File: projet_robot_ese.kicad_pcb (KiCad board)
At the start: 4 copper layers, 140 x 40 mm, 114 parts, among them J201 Conn_01x02, J202 Conn_01x04, J203 Conn_01x04, J204 Conn_01x04, J301 Conn_01x06, J302 Conn_01x06, J401 Conn_02x07_Odd_Even, J402 Conn_01x02, J403 Conn_01x02, J404 Conn_01x07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

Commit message: Last commit
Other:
- board text added: "RX"
- board text added: "TX"
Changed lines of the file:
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@@
     (property "Sheetname" "Stm32")
     (attr smd)
-    (fp_text reference "D404" (at 0 -1.43) (layer "F.SilkS")
+    (fp_text reference "D404" (at 0 -1.43) (layer "F.SilkS") hide
       (effects (font (size 1 1) (thickness 0.15)))
     )
@@
     (property "Sheetname" "Stm32")
     (attr smd)
-    (fp_text reference "D405" (at -0.046589 1.379618) (layer "F.SilkS")
+    (fp_text reference "D405" (at -0.046589 1.379618) (layer "F.SilkS") hide
       (effects (font (size 1 1) (thickness 0.15)))
     )
@@
     (property "Sheetname" "Stm32")
     (attr smd)
-    (fp_text reference "R413" (at 0 -1.43) (layer "F.SilkS")
+    (fp_text reference "R413" (at 0 -1.43) (layer "F.SilkS") hide
       (effects (font (size 1 1) (thickness 0.15)))
     )
@@
     (property "Sheetname" "Stm32")
     (attr smd)
-    (fp_text reference "R414" (at 0 1.5) (layer "F.SilkS")
+    (fp_text reference "R414" (at 0 1.5) (layer "F.SilkS") hide
       (effects (font (size 1 1) (thickness 0.15)))
     )
@@
   (gr_line (start 177 94.75) (end 177 103) (layer "F.SilkS") (width 0.15))
   (gr_rect (start 143 90) (end 148 92) (layer "F.SilkS") (width 0.15) (fill solid))
+  (gr_rect (start 141 109.75) (end 145 108.25) (layer "F.SilkS") (width 0.15) (fill solid))
   (gr_rect (start 192.5 116.75) (end 196.5 115.25) (layer "F.SilkS") (width 0.15) (fill solid))
   (gr_rect (start 129.75 111) (end 132.75 113) (layer "F.SilkS") (width 0.15) (fill solid))
@@
   (gr_rect (start 206.5 96) (end 208 100) (layer "F.SilkS") (width 0.15) (fill solid))
   (gr_rect (start 192.5 106.25) (end 196.5 104.75) (layer "F.SilkS") (width 0.15) (fill solid))
+  (gr_rect (start 146 109.75) (end 150 108.25) (layer "F.SilkS") (width 0.15) (fill solid))
   (gr_rect (start 201.5 106.25) (end 205.5 104.75) (layer "F.SilkS") (width 0.15) (fill solid))
   (gr_rect (start 192.5 111.5) (end 196.5 110) (layer "F.SilkS") (width 0.15) (fill solid))
@@
     (effects (font (size 1 1) (thickness 0.15)))
   )
+  (gr_text "TX" (at 148 109) (layer "F.Mask")
+    (effects (font (size 1 1) (thickness 0.15)))
+  )
   (gr_text "LED3" (at 207.25 98 90) (layer "F.Mask")
     (effects (font (size 1 1) (thickness 0.15)))
@@
     (effects (font (size 1 1) (thickness 0.15)))
   )
+  (gr_text "RX" (at 143 109) (layer "F.Mask")
+    (effects (font (size 1 1) (thickness 0.15)))
+  )

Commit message: Prof approved commit
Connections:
- net Net-(J201-Pad2) renamed /Power/BAT_IN
- net VBAT renamed UP_VBAT
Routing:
- net OUT1_1: track 8.55 -> 10.3 mm
- net /Driver moteur/V_BAT: track 150.7 -> 152.4 mm
- net STLINK_RX: track 46.2 -> 44.8 mm
- net GND: track 63.3 -> 62.6 mm
- net Net-(J302-Pad4): track 23.6 -> 23.0 mm
- net Net-(J301-Pad3): track 23.3 -> 24.0 mm
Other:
- board text added: "1"
- board text added: "2"
- board text added: "LED RX"
- board text added: "LED TX"
- board text removed: "COLOR"
- board text removed: "RX"
- board text removed: "TX"

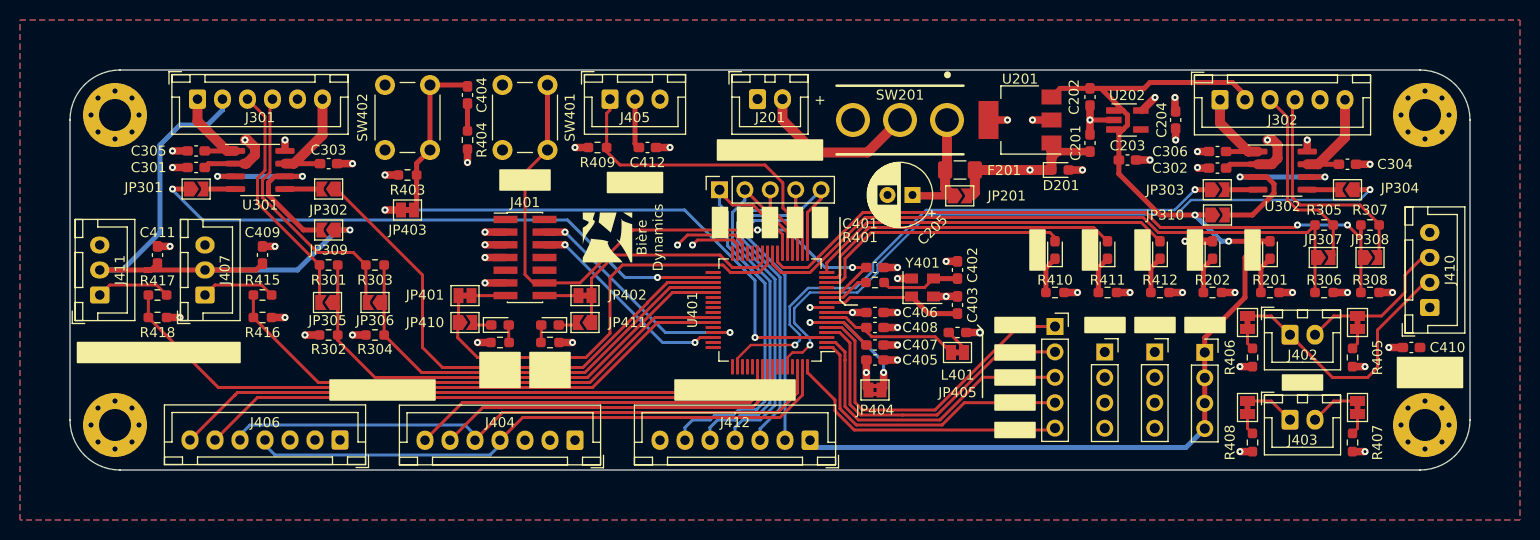
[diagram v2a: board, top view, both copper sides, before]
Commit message: I2C bus correction & simplifaction
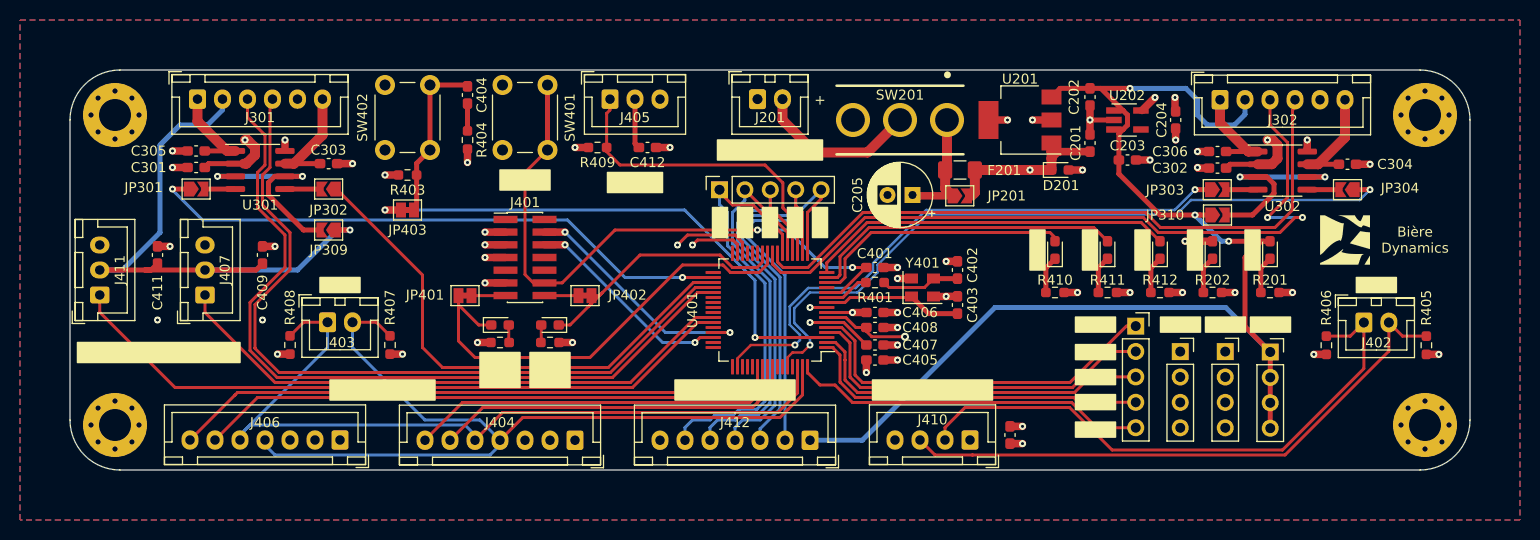
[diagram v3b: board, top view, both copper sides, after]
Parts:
- removed JP305, JP306, JP307, JP308, JP410, JP411: SolderJumper_2_Open, Jumper:SolderJumper-2_P1.3mm_Open_TrianglePad1.0x1.5mm
- removed JP404: SolderJumper_2_Bridged, Jumper:SolderJumper-2_P1.3mm_Bridged2Bar_Pad1.0x1.5mm
- removed JP405, JP406, JP407, JP408, JP409: SolderJumper_2_Bridged, Jumper:SolderJumper-2_P1.3mm_Bridged_Pad1.0x1.5mm
- removed L401: 600R @100MHz, Inductor_SMD:L_0603_1608Metric_Pad1.05x0.95mm_HandSolder
- removed R301, R303, R305, R307, R416, R418: 2k, Resistor_SMD:R_0603_1608Metric_Pad0.98x0.95mm_HandSolder
- removed R302, R304, R306, R308: 3k, Resistor_SMD:R_0603_1608Metric_Pad0.98x0.95mm_HandSolder
- removed R415, R417: 1k, Resistor_SMD:R_0603_1608Metric_Pad0.98x0.95mm_HandSolder
- moved J403 96.7 mm to (125.8, 105.2)
- moved R407 96.7 mm to (132.0, 107.5)
- moved R408 96.7 mm to (122.0, 107.5)
- moved G*** 73.8 mm to (227.5, 97.0), turned to 0 degrees
- moved J410 47.8 mm to (190.0, 117.0), turned to 180 degrees
- moved C410 41.1 mm to (194.0, 116.5), turned to 90 degrees
- moved J408 8.08 mm to (206.6, 105.6)
- moved J202 7.55 mm to (211.0, 108.2)
- moved J402 7.49 mm to (229.4, 105.2)
- moved R405 7.49 mm to (235.6, 107.5)
- moved R406 7.49 mm to (225.6, 107.5)
- moved J203 7.05 mm to (215.5, 108.2)
- moved J204 6.55 mm to (220.0, 108.2)
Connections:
- net Net-(JP403-Pad1) renamed /Stm32/FROM_USR_BTN
- C204 pad 1: VDD -> VREF
- C405 pad 1: VDD -> VREF
- C406 pad 1: VDD -> VREF
- C407 pad 1: UP_VBAT -> VREF
- C410 pad 1: VDD -> VREF
- D203 pad 2: VDD -> VREF
- D404 pad 1: Net-(D404-Pad1) -> STLINK_RX
- D405 pad 1: Net-(D405-Pad1) -> STLINK_TX
- J203 pad 1: VDD -> VREF
- J203 pad 2: VDD -> VREF
- J203 pad 3: VDD -> VREF
- J203 pad 4: VDD -> VREF
- J301 pad 3: Net-(J301-Pad3) -> /Driver moteur/ENCODER_1_B
- J301 pad 4: Net-(J301-Pad4) -> /Driver moteur/ENCODER_1_A
- J302 pad 3: Net-(J302-Pad3) -> /Driver moteur/ENCODER_2_B
- J302 pad 4: Net-(J302-Pad4) -> /Driver moteur/ENCODER_2_A
- J401 pad 3: VDD -> VREF
- J404 pad 2: VDD -> VREF
- J406 pad 2: VDD -> VREF
- J407 pad 1: Net-(J407-Pad1) -> PROX_1
- J410 pad 1: VDD -> VREF
- J411 pad 1: Net-(J411-Pad1) -> PROX_2
- R403 pad 1: VDD -> VREF
- R405 pad 1: VDD -> VREF
- R405 pad 2: Net-(JP409-Pad1) -> I2C2_SDA
- R406 pad 1: VDD -> VREF
- R406 pad 2: Net-(JP408-Pad1) -> I2C2_SDL
- R407 pad 1: VDD -> VREF
- R407 pad 2: Net-(JP407-Pad1) -> I2C1_SDA
- R408 pad 1: VDD -> VREF
- R408 pad 2: Net-(JP406-Pad1) -> I2C1_SDL
- R409 pad 1: VDD -> VREF
- R413 pad 2: VDD -> VREF
- R414 pad 2: VDD -> VREF
- U202 pad 5: VDD -> VREF
- U401 pad 6: UP_VBAT -> VREF
- U401 pad 8: VDD -> VREF
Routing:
- net I2C1_SDL: track 151.4 -> 79.7 mm
- net I2C1_SDA: track 149.6 -> 84.7 mm
- net /Driver moteur/ENCODER_1_A: track 44.6 -> 77.9 mm
- net VDD: track 28.1 -> 0.00 mm, vias 16 -> 0
- net /Driver moteur/ENCODER_1_B: track 51.7 -> 79.7 mm
- net Net-(J301-Pad4): track 27.2 -> 0.00 mm
- net VREF: track 14.1 -> 40.2 mm, vias 0 -> 17
- net Net-(J301-Pad3): track 24.0 -> 0.00 mm
- net Net-(J302-Pad4): track 23.0 -> 0.00 mm
- net Net-(J302-Pad3): track 19.7 -> 0.00 mm
- net UP_VBAT: track 18.4 -> 0.00 mm, vias 2 -> 0
- net +5V: track 235.2 -> 250.9 mm, vias 3 -> 4
- net /Driver moteur/ENCODER_2_B: track 65.4 -> 74.8 mm, vias 0 -> 2
- net I2C2_SDA: track 90.0 -> 98.9 mm
- net PC10: track 27.6 -> 35.1 mm
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- added copper zone on In2.Cu, net VREF
- removed copper zone on In2.Cu, net VDD
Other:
- board text added: "I2C1"
- board text added: "I2C2"
- board text removed: "I2Cs"
